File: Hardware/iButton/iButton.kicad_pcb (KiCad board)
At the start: 2 copper layers, 15.8 x 24.3 mm, 29 parts, among them IC1 TSOP75338TR, J1 Conn_01x06, X1b1 PG-2.5-9.5-SM, X2b1 PG-2.5-8.0-SM, X3b1 PG-3.0-10.0-SM

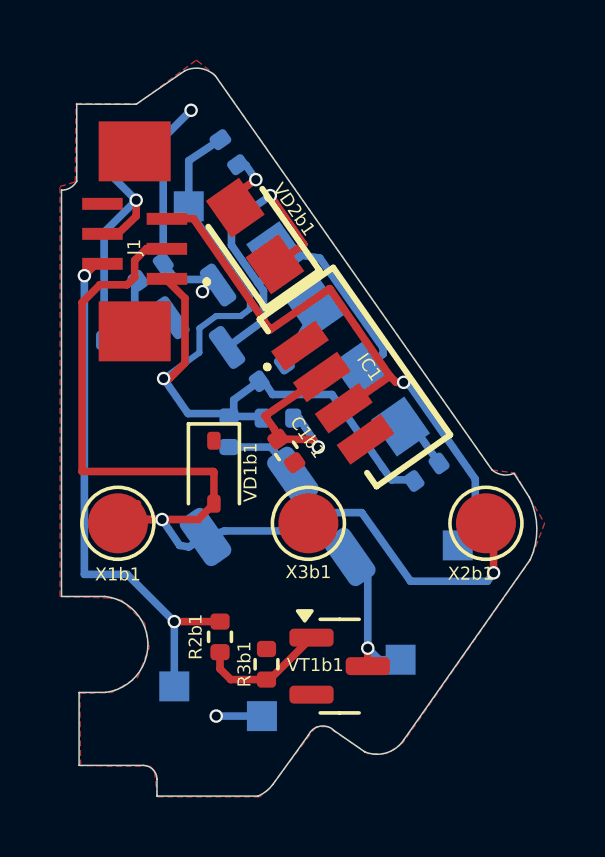
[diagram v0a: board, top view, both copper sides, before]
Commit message: PCB: iButton PCB finetune corner
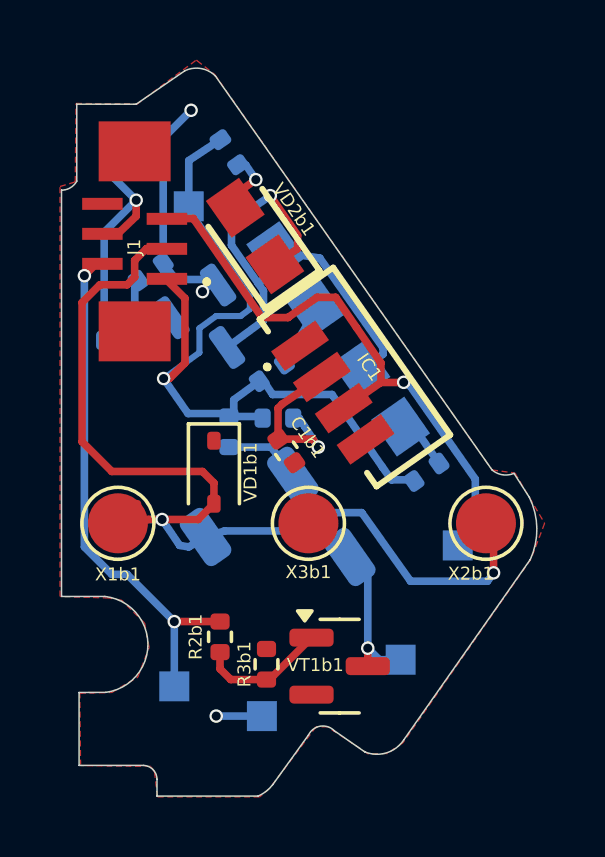
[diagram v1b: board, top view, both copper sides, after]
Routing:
- net /iButton: track 35.5 -> 34.7 mm
- net /IR_RX: track 21.1 -> 20.5 mm
- net /SPEAKER: track 18.0 -> 17.4 mm
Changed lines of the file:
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@@
+	)
+	(segment
+		(start 160.6804 91.9988)
+		(end 160.6804 92.5576)
+		(width 0.254)
+		(layer "F.Cu")
+		(net 3)
 	)
 	(segment
@@
 	)
 	(segment
+		(start 158.9278 93.4037)
+		(end 158.9278 98.044)
+		(width 0.254)
+		(layer "F.Cu")
+		(net 3)
+	)
+	(segment
 		(start 159.5199 92.8116)
 		(end 158.9278 93.4037)
@@
 	)
 	(segment
-		(start 160.6804 91.9988)
-		(end 160.6804 92.5576)
-		(width 0.254)
-		(layer "F.Cu")
-		(net 3)
-	)
-	(segment
-		(start 158.9278 99.0346)
-		(end 163.2966 99.0346)
-		(width 0.254)
-		(layer "F.Cu")
-		(net 3)
-	)
-	(segment
 		(start 161.5948 100.6348)
 		(end 162.7972 100.6348)
@@
 	)
 	(segment
+		(start 160.7734 100.11)
+		(end 160.1216 100.7618)
+		(width 0.254)
+		(layer "F.Cu")
+		(net 3)
+	)
+	(segment
+		(start 162.941 99.0346)
+		(end 163.322 99.4156)
+		(width 0.254)
+		(layer "F.Cu")
+		(net 3)
+	)
+	(segment
+		(start 160.6804 92.5576)
+		(end 160.4264 92.8116)
+		(width 0.254)
+		(layer "F.Cu")
+		(net 3)
+	)
+	(segment
+		(start 172.6438 102.4128)
+		(end 172.6438 100.7618)
+		(width 0.254)
+		(layer "F.Cu")
+		(net 3)
+	)
+	(segment
+		(start 159.9184 99.0346)
+		(end 162.941 99.0346)
+		(width 0.254)
+		(layer "F.Cu")
+		(net 3)
+	)
+	(segment
+		(start 161.671 91.6018)
+		(end 161.0774 91.6018)
+		(width 0.254)
+		(layer "F.Cu")
+		(net 3)
+	)
+	(segment
+		(start 162.7972 100.6348)
+		(end 163.322 100.11)
+		(width 0.254)
+		(layer "F.Cu")
+		(net 3)
+	)
+	(segment
+		(start 163.322 99.4156)
+		(end 163.322 100.11)
+		(width 0.254)
+		(layer "F.Cu")
+		(net 3)
+	)
+	(segment
+		(start 158.9278 98.044)
+		(end 159.9184 99.0346)
+		(width 0.254)
+		(layer "F.Cu")
+		(net 3)
+	)
+	(segment
 		(start 161.0774 91.6018)
 		(end 160.6804 91.9988)
@@
 	)
 	(segment
-		(start 158.9278 93.4037)
-		(end 158.9278 99.0346)
-		(width 0.254)
-		(layer "F.Cu")
-		(net 3)
-	)
-	(segment
-		(start 161.671 91.6018)
-		(end 161.0774 91.6018)
-		(width 0.254)
-		(layer "F.Cu")
-		(net 3)
-	)
-	(segment
 		(start 160.4264 92.8116)
 		(end 159.5199 92.8116)
@@
 	)
 	(segment
-		(start 160.7734 100.11)
-		(end 160.1216 100.7618)
-		(width 0.254)
-		(layer "F.Cu")
-		(net 3)
-	)
-	(segment
-		(start 163.2966 99.0346)
-		(end 163.322 99.06)
-		(width 0.254)
-		(layer "F.Cu")
-		(net 3)
-	)
-	(segment
-		(start 172.6438 102.4128)
-		(end 172.6438 100.7618)
-		(width 0.254)
-		(layer "F.Cu")
-		(net 3)
-	)
-	(segment
-		(start 163.322 99.06)
-		(end 163.322 100.11)
-		(width 0.254)
-		(layer "F.Cu")
-		(net 3)
-	)
-	(segment
-		(start 162.7972 100.6348)
-		(end 163.322 100.11)
-		(width 0.254)
-		(layer "F.Cu")
-		(net 3)
-	)
-	(segment
 		(start 161.5948 100.6348)
 		(end 161.1376 100.6348)
@@
 		(net 3)
 	)
-	(segment
-		(start 160.6804 92.5576)
-		(end 160.4264 92.8116)
-		(width 0.254)
-		(layer "F.Cu")
-		(net 3)
-	)
 	(via
 		(at 172.6438 102.4128)
@@
 	)
 	(segment
-		(start 166.624 97.9678)
-		(end 165.459683 97.955607)
+		(start 165.459683 96.925981)
+		(end 165.597132 96.788532)
 		(width 0.254)
 		(layer "F.Cu")
@@
 	)
 	(segment
-		(start 165.3286 97.6122)
-		(end 165.459683 97.955607)
+		(start 165.459683 97.955607)
+		(end 165.459683 96.925981)
 		(width 0.254)
 		(layer "F.Cu")
@@
 	)
 	(segment
-		(start 165.0238 97.1804)
-		(end 165.3286 97.6122)
+		(start 165.459683 97.955607)
+		(end 166.611807 97.955607)
+		(width 0.254)
+		(layer "F.Cu")
+		(net 5)
+	)
+	(segment
+		(start 166.611807 97.955607)
+		(end 166.624 97.9678)
 		(width 0.254)
 		(layer "F.Cu")
@@
 	(segment
 		(start 166.920642 95.883923)
-		(end 165.0238 97.1804)
+		(end 165.597132 96.788532)
 		(width 0.254)
 		(layer "F.Cu")
@@
 	)
 	(segment
-		(start 162.6362 90.6018)
-		(end 165.2016 94.3102)
-		(width 0.254)
-		(layer "F.Cu")
-		(net 6)
-	)
-	(segment
-		(start 167.1828 92.9386)
-		(end 168.0718 94.234)
+		(start 165.7917 93.904828)
+		(end 165.801964 93.894564)
 		(width 0.254)
 		(layer "F.Cu")
@@
 	)
 	(segment
+		(start 162.6362 90.6018)
+		(end 164.921172 93.904828)
+		(width 0.254)
+		(layer "F.Cu")
+		(net 6)
+	)
+	(segment
+		(start 166.762546 93.229546)
+		(end 167.379234 93.229546)
+		(width 0.254)
+		(layer "F.Cu")
+		(net 6)
+	)
+	(segment
+		(start 168.889019 96.067219)
+		(end 168.889019 95.413405)
+		(width 0.254)
+		(layer "F.Cu")
+		(net 6)
+	)
+	(segment
 		(start 169.6466 96.0628)
-		(end 169.3926 96.0628)
-		(width 0.254)
-		(layer "F.Cu")
-		(net 6)
-	)
-	(segment
-		(start 165.2016 94.3102)
-		(end 167.1828 92.9386)
-		(width 0.254)
-		(layer "F.Cu")
-		(net 6)
-	)
-	(segment
-		(start 169.3926 96.0628)
-		(end 169.1894 95.8596)
+		(end 169.642181 96.067219)
+		(width 0.254)
+		(layer "F.Cu")
+		(net 6)
+	)
+	(segment
+		(start 165.801964 93.894564)
+		(end 166.762546 93.229546)
 		(width 0.254)
 		(layer "F.Cu")
@@
 	(segment
 		(start 167.649084 96.924246)
-		(end 169.1894 95.8596)
-		(width 0.254)
-		(layer "F.Cu")
-		(net 6)
-	)
-	(segment
-		(start 169.1894 95.8596)
+		(end 168.889019 96.067219)
+		(width 0.254)
+		(layer "F.Cu")
+		(net 6)
+	)
+	(segment
+		(start 164.921172 93.904828)
+		(end 165.7917 93.904828)
+		(width 0.254)
+		(layer "F.Cu")
+		(net 6)
+	)
+	(segment
+		(start 167.389544 93.239856)
+		(end 168.0718 94.234)
+		(width 0.254)
+		(layer "F.Cu")
+		(net 6)
+	)
+	(segment
+		(start 168.889019 95.413405)
+		(end 168.868607 95.392993)
+		(width 0.254)
+		(layer "F.Cu")
+		(net 6)
+	)
+	(segment
+		(start 168.868607 95.392993)
 		(end 168.0718 94.234)
 		(width 0.254)
@@
 		(start 161.671 90.6018)
 		(end 162.6362 90.6018)
+		(width 0.254)
+		(layer "F.Cu")
+		(net 6)
+	)
+	(segment
+		(start 167.379234 93.229546)
+		(end 167.389544 93.239856)
+		(width 0.254)
+		(layer "F.Cu")
+		(net 6)
+	)
+	(segment
+		(start 169.642181 96.067219)
+		(end 168.889019 96.067219)
 		(width 0.254)
 		(layer "F.Cu")
@@
 	)
 	(segment
-		(start 159.004 102.4636)
+		(start 159.004 92.5068)
+		(end 159.004 101.5492)
+		(width 0.254)
+		(layer "B.Cu")
+		(net 9)
+	)
+	(segment
+		(start 159.9184 102.4636)
 		(end 160.4264 102.4636)
-		(width 0.254)
-		(layer "B.Cu")
-		(net 9)
-	)
-	(segment
-		(start 159.004 92.5068)
-		(end 159.004 102.4636)
 		(width 0.254)
 		(layer "B.Cu")
@@
 	)
 	(segment
+		(start 159.004 101.5492)
+		(end 159.9184 102.4636)
+		(width 0.254)
+		(layer "B.Cu")
+		(net 9)
+	)
+	(segment
 		(start 162.0012 106.1974)
 		(end 162.0012 104.0384)
@@
 	)
 	(segment
+		(start 166.112237 91.164363)
+		(end 165.2016 89.8398)
+		(width 0.254)
+		(layer "F.Cu")
+		(net 15)
+	)
+	(segment
 		(start 165.353213 92.128025)
-		(end 166.3192 91.4654)
+		(end 166.093216 91.620416)
 		(width 0.254)
 		(layer "F.Cu")
@@
 	)
 	(segment
-		(start 166.3192 91.4654)
-		(end 165.2016 89.8398)
-		(width 0.254)
-		(layer "F.Cu")
+		(start 166.112237 91.164363)
+		(end 166.112237 91.601395)
+		(width 0.254)
+		(layer "F.Cu")
+		(net 15)
+	)
+	(segment
+		(start 166.112237 91.601395)
+		(end 166.093216 91.620416)
+		(width 0.254)
+		(layer "F.Cu")
